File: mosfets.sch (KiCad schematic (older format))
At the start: 38 parts, among them Q1 IXFK300N20X3, Q2 IXFK300N20X3, Q3 IXFK300N20X3, Q4 IXFK300N20X3, Q5 IXFK300N20X3, Q6 IXFK300N20X3, U1 ACS781xLRTR-150B, U2 ACS781xLRTR-150B, U3 ACS781xLRTR-150B

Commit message: - updated schematic symbols - updated silk screen version label
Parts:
- C14, C15, C17, C18, C19: symbol Device:CP -> Device:C_Polarized
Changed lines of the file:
@@
 $EndComp
 $Comp
-L Device:CP C15
+L Device:C_Polarized C15
 U 1 1 58A7B8F0
 P 3200 7150
@@
 	8300 3650 8950 3650
 $Comp
-L Device:CP C17
+L Device:C_Polarized C17
 U 1 1 5C9BC25E
 P 3450 7150
@@
 $EndComp
 $Comp
-L Device:CP C18
+L Device:C_Polarized C18
 U 1 1 5C9BC29A
 P 3700 7150
@@
 $EndComp
 $Comp
-L Device:CP C19
+L Device:C_Polarized C19
 U 1 1 5C9BD172
 P 3950 7150
@@
 $EndComp
 $Comp
-L Device:CP C14
+L Device:C_Polarized C14
 U 1 1 5C9BD1B2
 P 2950 7150

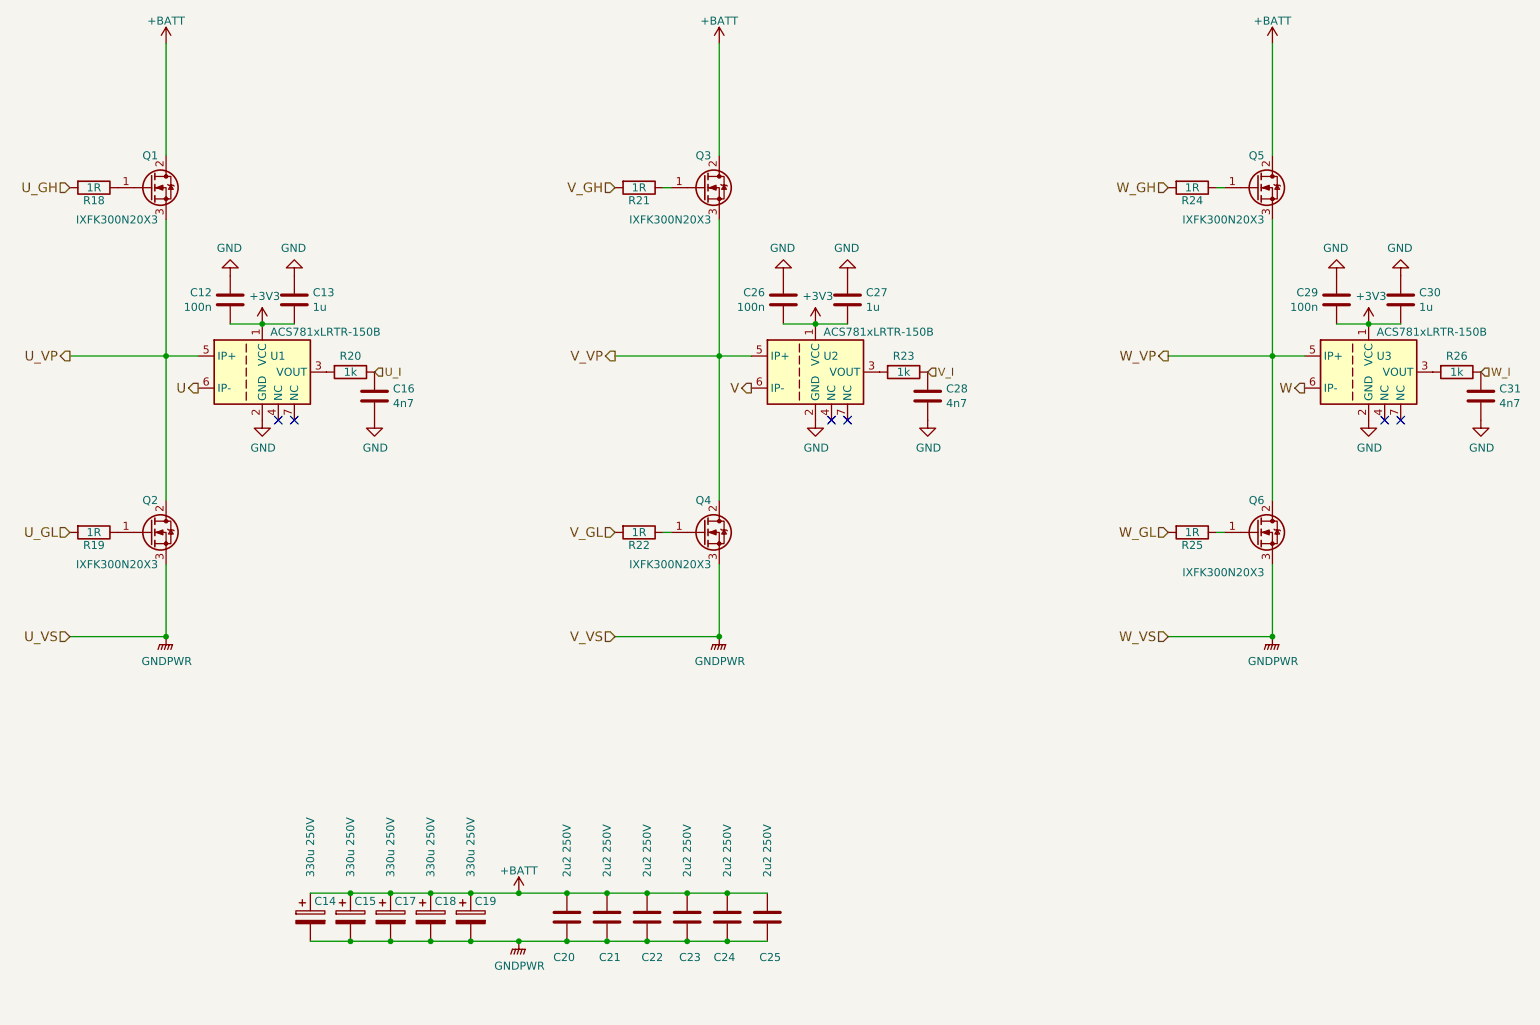
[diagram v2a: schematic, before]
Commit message: - changed gate resistors to 4R7
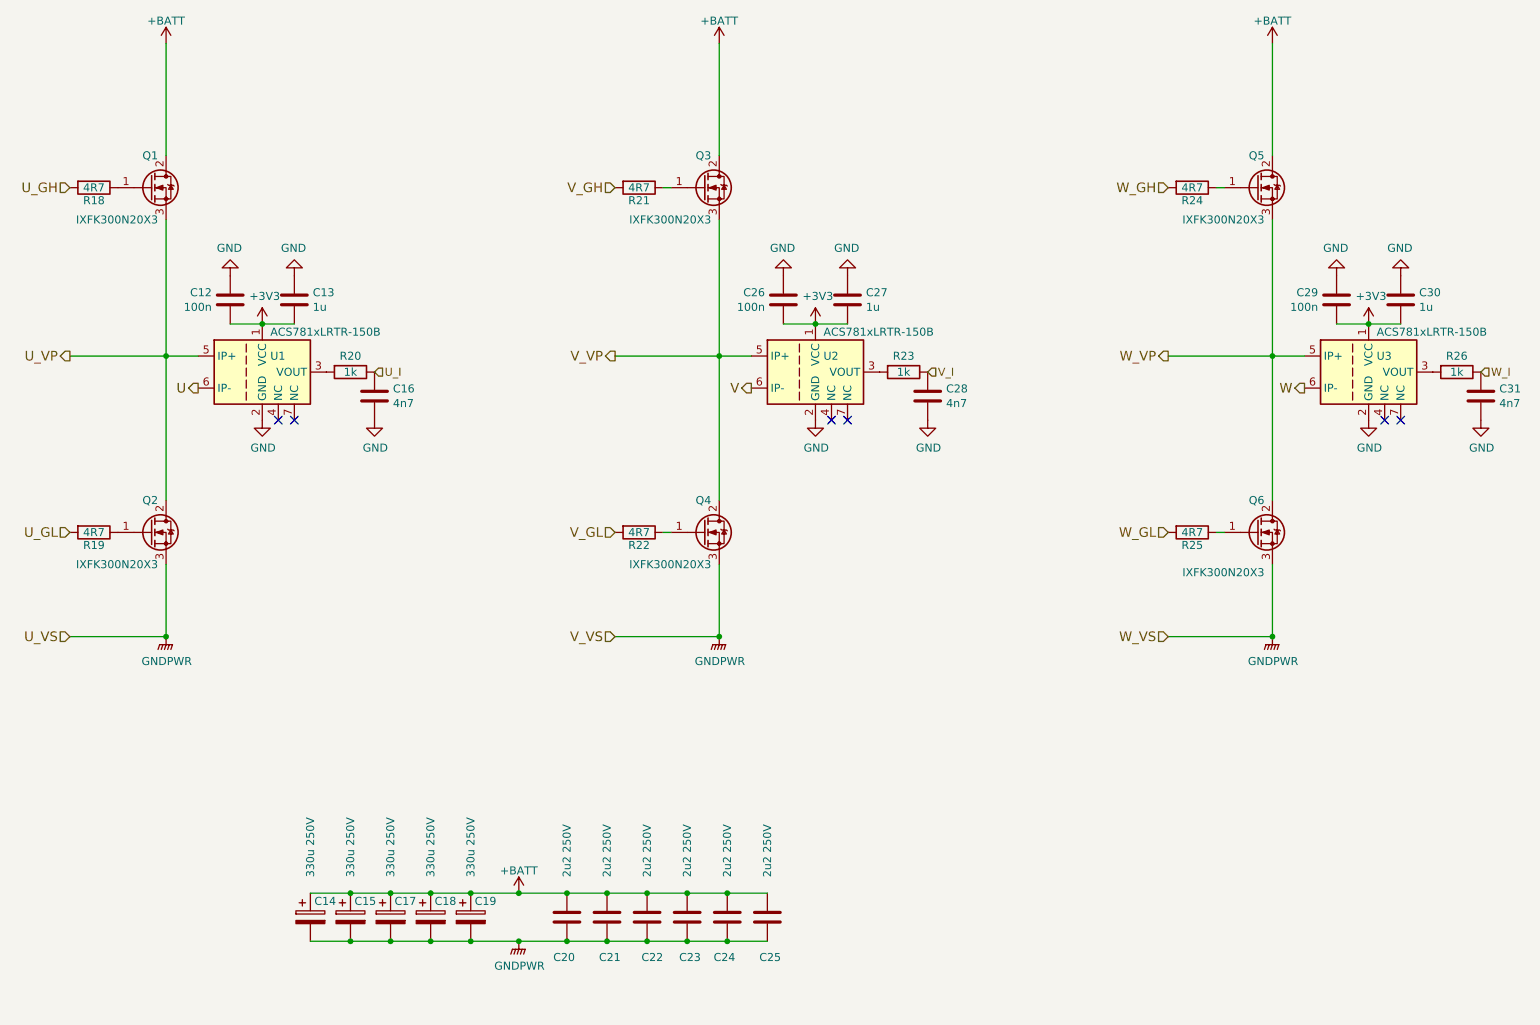
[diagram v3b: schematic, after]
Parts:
- R18, R19, R21, R22, R24, R25: value 1R -> 4R7
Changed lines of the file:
@@
 P 8450 4750
 F 0 "R25" V 8530 4750 50  0000 C CNN
-F 1 "1R" V 8450 4750 50  0000 C CNN
+F 1 "4R7" V 8450 4750 50  0000 C CNN
 F 2 "Resistor_SMD:R_0805_2012Metric" V 8380 4750 50  0001 C CNN
 F 3 "" H 8450 4750 50  0000 C CNN
@@
 P 8450 2600
 F 0 "R24" V 8530 2600 50  0000 C CNN
-F 1 "1R" V 8450 2600 50  0000 C CNN
+F 1 "4R7" V 8450 2600 50  0000 C CNN
 F 2 "Resistor_SMD:R_0805_2012Metric" V 8380 2600 50  0001 C CNN
 F 3 "" H 8450 2600 50  0000 C CNN
@@
 P 5000 4750
 F 0 "R22" V 5080 4750 50  0000 C CNN
-F 1 "1R" V 5000 4750 50  0000 C CNN
+F 1 "4R7" V 5000 4750 50  0000 C CNN
 F 2 "Resistor_SMD:R_0805_2012Metric" V 4930 4750 50  0001 C CNN
 F 3 "" H 5000 4750 50  0000 C CNN
@@
 P 5000 2600
 F 0 "R21" V 5080 2600 50  0000 C CNN
-F 1 "1R" V 5000 2600 50  0000 C CNN
+F 1 "4R7" V 5000 2600 50  0000 C CNN
 F 2 "Resistor_SMD:R_0805_2012Metric" V 4930 2600 50  0001 C CNN
 F 3 "" H 5000 2600 50  0000 C CNN
@@
 P 1600 4750
 F 0 "R19" V 1680 4750 50  0000 C CNN
-F 1 "1R" V 1600 4750 50  0000 C CNN
+F 1 "4R7" V 1600 4750 50  0000 C CNN
 F 2 "Resistor_SMD:R_0805_2012Metric" V 1530 4750 50  0001 C CNN
 F 3 "" H 1600 4750 50  0000 C CNN
@@
 P 1600 2600
 F 0 "R18" V 1680 2600 50  0000 C CNN
-F 1 "1R" V 1600 2600 50  0000 C CNN
+F 1 "4R7" V 1600 2600 50  0000 C CNN
 F 2 "Resistor_SMD:R_0805_2012Metric" V 1530 2600 50  0001 C CNN
 F 3 "" H 1600 2600 50  0000 C CNN
